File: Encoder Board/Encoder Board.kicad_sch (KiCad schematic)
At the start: 18 parts, among them J1 Conn_02x05_Odd_Even, J2 Conn_02x05_Odd_Even, J3 Conn_01x01_Pin, J4 Conn_01x01_Pin, U1 AM26LV32xD

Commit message: Add descriptive labels to silkscreen
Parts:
- removed J3, J4: Conn_01x01_Pin, Connector_PinHeader_2.54mm:PinHeader_1x01_P2.54mm_Vertical, symbol Connector:Conn_01x01_Pin
- added J3, J4: Conn_01x02_Pin, Connector_PinHeader_2.54mm:PinHeader_1x02_P2.54mm_Vertical, symbol Connector:Conn_01x02_Pin
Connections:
- net +5V_S: now also J3.1 (Pin_1)
- net GND: now also J3.2 (Pin_2), J4.2 (Pin_2)
- net TRIGGER: now also J4.1 (Pin_1)
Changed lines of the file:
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@@
 	)
 	(symbol
-		(lib_id "Connector:Conn_01x01_Pin")
+		(lib_id "Connector:Conn_01x02_Pin")
 		(at 93.98 22.86 0)
 		(unit 1)
@@
 		(dnp no)
 		(fields_autoplaced yes)
-		(property "Reference" "J4"
+		(property "Reference" "J3"
 			(at 94.615 17.78 0)
 			(show_name no)
@@
 			)
 		)
-		(property "Value" "Conn_01x01_Pin"
+		(property "Value" "Conn_01x02_Pin"
 			(at 94.615 20.32 0)
 			(show_name no)
@@
 			)
 		)
-		(property "Footprint" "Connector_PinHeader_2.54mm:PinHeader_1x01_P2.54mm_Vertical"
+		(property "Footprint" "Connector_PinHeader_2.54mm:PinHeader_1x02_P2.54mm_Vertical"
 			(at 93.98 22.86 0)
 			(hide yes)
@@
 			)
 		)
-		(property "Description" "Generic connector, single row, 01x01, script generated"
+		(property "Description" "Generic connector, single row, 01x02, script generated"
 			(at 93.98 22.86 0)
 			(hide yes)
@@
 		(pin "1"
 		)
-		(instances
-			(project "Encoder Board"
-				(path "/b150f569-1eb1-4e1b-95b0-6f55a9bdc5c1"
-					(reference "J4")
+		(pin "2"
+		)
+		(instances
+			(project "Encoder Board"
+				(path "/b150f569-1eb1-4e1b-95b0-6f55a9bdc5c1"
+					(reference "J3")
 					(unit 1)
 				)
@@
 	)
 	(symbol
-		(lib_id "Connector:Conn_01x01_Pin")
-		(at 219.71 64.77 180)
-		(unit 1)
-		(body_style 1)
-		(exclude_from_sim no)
-		(in_bom yes)
-		(on_board yes)
-		(in_pos_files yes)
-		(dnp no)
-		(fields_autoplaced yes)
-		(property "Reference" "J3"
-			(at 219.075 59.69 0)
-			(show_name no)
-			(do_not_autoplace no)
-			(effects
-				(font
-					(size 1.27 1.27)
-				)
-			)
-		)
-		(property "Value" "Conn_01x01_Pin"
-			(at 219.075 62.23 0)
-			(show_name no)
-			(do_not_autoplace no)
-			(effects
-				(font
-					(size 1.27 1.27)
-				)
-			)
-		)
-		(property "Footprint" "Connector_PinHeader_2.54mm:PinHeader_1x01_P2.54mm_Vertical"
+		(lib_id "Connector:Conn_01x02_Pin")
+		(at 219.71 64.77 0)
+		(mirror y)
+		(unit 1)
+		(body_style 1)
+		(exclude_from_sim no)
+		(in_bom yes)
+		(on_board yes)
+		(in_pos_files yes)
+		(dnp no)
+		(property "Reference" "J4"
+			(at 220.98 67.3101 0)
+			(show_name no)
+			(do_not_autoplace no)
+			(effects
+				(font
+					(size 1.27 1.27)
+				)
+				(justify right)
+			)
+		)
+		(property "Value" "Conn_01x02_Pin"
+			(at 220.98 64.7701 0)
+			(show_name no)
+			(do_not_autoplace no)
+			(effects
+				(font
+					(size 1.27 1.27)
+				)
+				(justify right)
+			)
+		)
+		(property "Footprint" "Connector_PinHeader_2.54mm:PinHeader_1x02_P2.54mm_Vertical"
 			(at 219.71 64.77 0)
 			(hide yes)
@@
 			)
 		)
-		(property "Description" "Generic connector, single row, 01x01, script generated"
+		(property "Description" "Generic connector, single row, 01x02, script generated"
 			(at 219.71 64.77 0)
 			(hide yes)
@@
 		(pin "1"
 		)
-		(instances
-			(project "Encoder Board"
-				(path "/b150f569-1eb1-4e1b-95b0-6f55a9bdc5c1"
-					(reference "J3")
+		(pin "2"
+		)
+		(instances
+			(project "Encoder Board"
+				(path "/b150f569-1eb1-4e1b-95b0-6f55a9bdc5c1"
+					(reference "J4")
 					(unit 1)
 				)
@@
 					(unit 1)
 				)
+			)
+		)
+	)
+	(symbol
+		(lib_id "power:GND")
+		(at 214.63 67.31 0)
+		(unit 1)
+		(body_style 1)
+		(exclude_from_sim no)
+		(in_bom yes)
+		(on_board yes)
+		(in_pos_files yes)
+		(dnp no)
+		(fields_autoplaced yes)
+		(property "Reference" "#PWR012"
+			(at 214.63 73.66 0)
+			(hide yes)
+			(show_name no)
+			(do_not_autoplace no)
+			(effects
+				(font
+					(size 1.27 1.27)
+				)
+			)
+		)
+		(property "Value" "GND"
+			(at 214.63 72.39 0)
+			(show_name no)
+			(do_not_autoplace no)
+			(effects
+				(font
+					(size 1.27 1.27)
+				)
+			)
+		)
+		(property "Footprint" ""
+			(at 214.63 67.31 0)
+			(hide yes)
+			(show_name no)
+			(do_not_autoplace no)
+			(effects
+				(font
+					(size 1.27 1.27)
+				)
+			)
+		)
+		(property "Datasheet" ""
+			(at 214.63 67.31 0)
+			(hide yes)
+			(show_name no)
+			(do_not_autoplace no)
+			(effects
+				(font
+					(size 1.27 1.27)
+				)
+			)
+		)
+		(property "Description" "Power symbol creates a global label with name \"GND\" , ground"
+			(at 214.63 67.31 0)
+			(hide yes)
+			(show_name no)
+			(do_not_autoplace no)
+			(effects
+				(font
+					(size 1.27 1.27)
+				)
+			)
+		)
+		(pin "1"
+		)
+		(instances
+			(project "Encoder Board"
+				(path "/b150f569-1eb1-4e1b-95b0-6f55a9bdc5c1"
+					(reference "#PWR012")
+					(unit 1)
+				)
+			)
+		)
+	)
+	(symbol
+		(lib_id "power:GND")
+		(at 99.06 25.4 0)
+		(unit 1)
+		(body_style 1)
+		(exclude_from_sim no)
+		(in_bom yes)
+		(on_board yes)
+		(in_pos_files yes)
+		(dnp no)
+		(fields_autoplaced yes)
+		(property "Reference" "#PWR013"
+			(at 99.06 31.75 0)
+			(hide yes)
+			(show_name no)
+			(do_not_autoplace no)
+			(effects
+				(font
+					(size 1.27 1.27)
+				)
+			)
+		)
+		(property "Value" "GND"
+			(at 99.06 30.48 0)
+			(show_name no)
+			(do_not_autoplace no)
+			(effects
+				(font
+					(size 1.27 1.27)
+				)
+			)
+		)
+		(property "Footprint" ""
+			(at 99.06 25.4 0)
+			(hide yes)
+			(show_name no)
+			(do_not_autoplace no)
+			(effects
+				(font
+					(size 1.27 1.27)
+				)
+			)
+		)
+		(property "Datasheet" ""
+			(at 99.06 25.4 0)
+			(hide yes)
+			(show_name no)
+			(do_not_autoplace no)
+			(effects
+				(font
+					(size 1.27 1.27)
+				)
+			)
+		)
+		(property "Description" "Power symbol creates a global label with name \"GND\" , ground"
+			(at 99.06 25.4 0)
+			(hide yes)
+			(show_name no)
+			(do_not_autoplace no)
+			(effects
+				(font
+					(size 1.27 1.27)
+				)
+			)
+		)
+		(pin "1"
+		)
+		(instances
+			(project "Encoder Board"
+				(path "/b150f569-1eb1-4e1b-95b0-6f55a9bdc5c1"
+					(reference "#PWR013")
+					(unit 1)
+				)

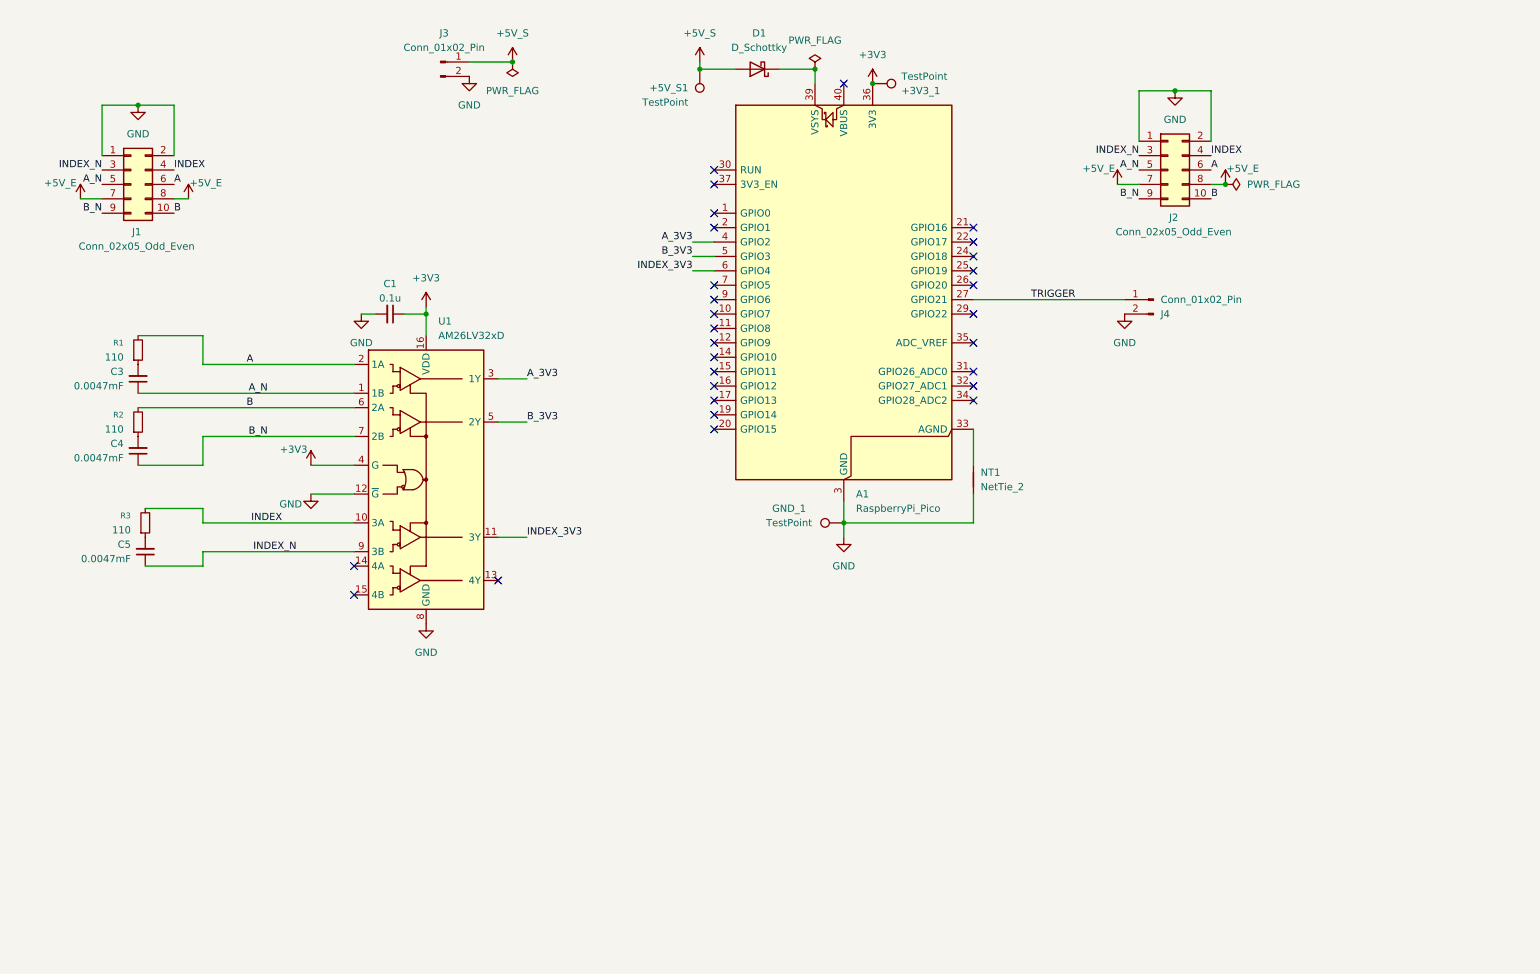
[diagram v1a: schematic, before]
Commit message: change pico footprint, make extra GPIO pins available, re-route and place components, add power pours and stitching vias
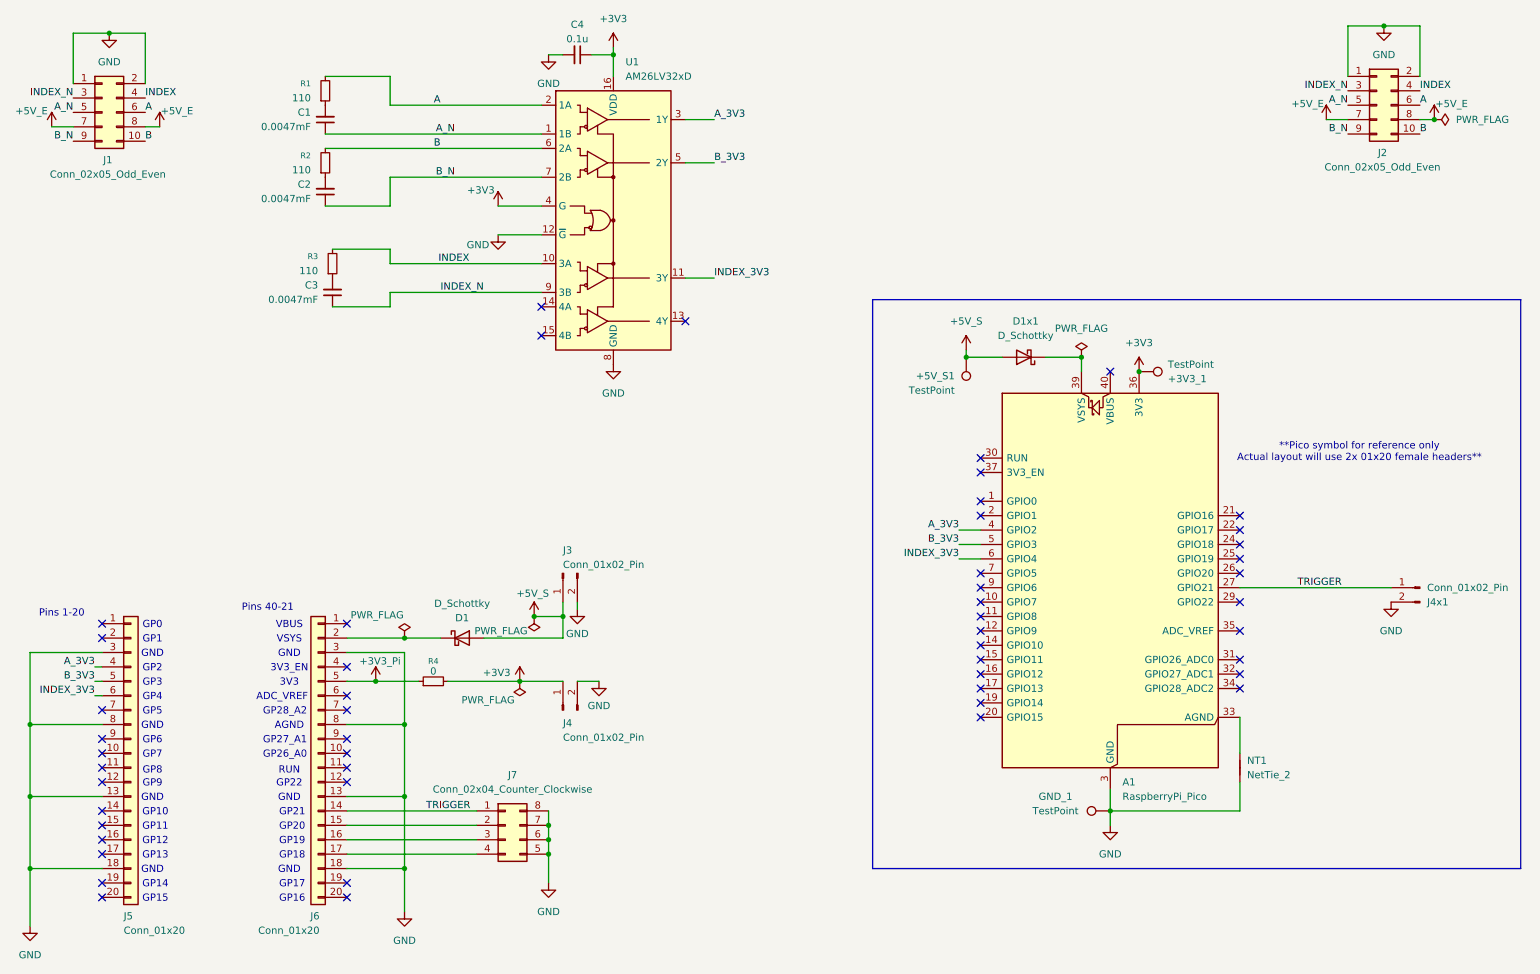
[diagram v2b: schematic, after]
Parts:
- added D1: D_Schottky, Diode_SMD:D_SMA_Handsoldering, symbol Device:D_Schottky
- added J4: Conn_01x02_Pin, Connector_PinHeader_2.54mm:PinHeader_1x02_P2.54mm_Vertical, symbol Connector:Conn_01x02_Pin
- added J5, J6: Conn_01x20, Connector_PinSocket_2.54mm:PinSocket_1x20_P2.54mm_Vertical, symbol Connector_Generic:Conn_01x20
- added J7: Conn_02x04_Counter_Clockwise, Connector_PinHeader_2.54mm:PinHeader_2x04_P2.54mm_Vertical, symbol Connector_Generic:Conn_02x04_Counter_Clockwise
- added R4: 0, Resistor_SMD:R_0805_2012Metric_Pad1.20x1.40mm_HandSolder, symbol Device:R_Small
- renumbered C3 to C1, C4 to C2, C5 to C3, C1 to C4, D1 to D1x1, J4 to J4x1
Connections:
- net +3V3: now also J4.1 (Pin_1), R4.2
- net +5V_S: now also D1.2 (A)
- net A_3V3: now also J5.4 (Pin_4)
- net B_3V3: now also J5.5 (Pin_5)
- net GND: now also J4.2 (Pin_2), J5.13 (Pin_13), J5.18 (Pin_18), J5.3 (Pin_3), J5.8 (Pin_8), J6.13 (Pin_13), J6.18 (Pin_18), J6.3 (Pin_3), J6.8 (Pin_8), J7.5 (Pin_5), J7.6 (Pin_6), J7.7 (Pin_7), J7.8 (Pin_8)
- net INDEX_3V3: now also J5.6 (Pin_6)
- net TRIGGER: now also J6.14 (Pin_14), J7.1 (Pin_1)
- new net: D1.1 (K), J6.2 (Pin_2)
- new net: J6.15 (Pin_15), J7.2 (Pin_2)
- new net: J6.16 (Pin_16), J7.3 (Pin_3)
- new net: J6.17 (Pin_17), J7.4 (Pin_4)
- new net +3V3_Pi: J6.5 (Pin_5), R4.1
- no-connect marks 29 -> 52
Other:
- note added: "**Pico symbol for reference only Actual layout will use 2x 01x20 female headers**"
- note added: "3V3"
- note added: "3V3_EN"
- note added: "ADC_VREF"
- note added: "AGND"
- note added: "GND"
- note added: "GP0"
- note added: "GP1"
- note added: "GP10"
- note added: "GP11"
- note added: "GP12"
- note added: "GP13"
- note added: "GP14"
- note added: "GP15"
- note added: "GP16"
- note added: "GP17"
- note added: "GP18"
- note added: "GP19"
- note added: "GP2"
- note added: "GP20"
- note added: "GP21"
- note added: "GP22"
- note added: "GP26_A0"
- note added: "GP27_A1"
- note added: "GP28_A2"
- note added: "GP3"
- note added: "GP4"
- note added: "GP5"
- note added: "GP6"
- note added: "GP7"
- note added: "GP8"
- note added: "GP9"
- note added: "Pins 1-20"
- note added: "Pins 40-21"
- note added: "RUN"
- note added: "VBUS"
- note added: "VSYS"
- moved on the sheet: +3V3_1, +5V_S1, A1, C1, C2, C3, C4, D1x1, GND_1, J1, J2, J3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
